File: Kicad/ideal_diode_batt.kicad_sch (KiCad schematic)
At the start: 8 parts, among them Q3 AON7422G, U7 LM74700QDBVTQ1

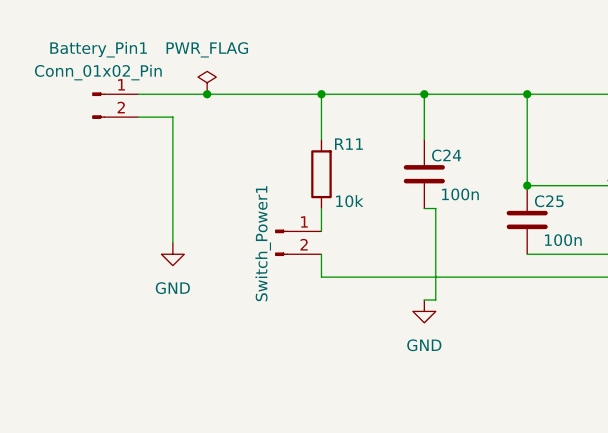
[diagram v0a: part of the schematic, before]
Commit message: finished pcb - added pwm resistors, and fixed VDDA decoupling
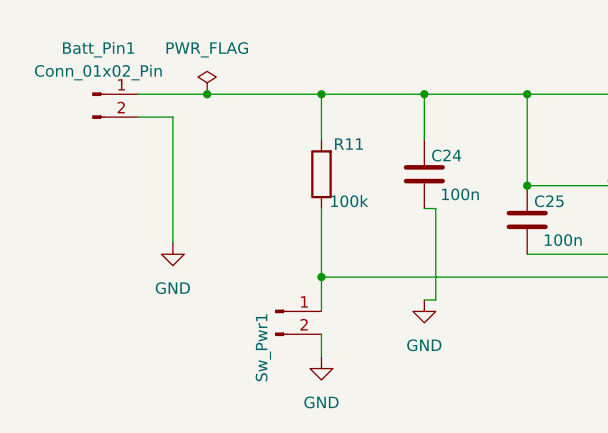
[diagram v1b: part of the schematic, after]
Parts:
- R11: value 10k -> 100k
- renumbered Battery_Pin1 to Batt_Pin1, Switch_Power1 to Sw_Pwr1
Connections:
- net EN: now also R11.1, Sw_Pwr1.1 (Pin_1); no longer Sw_Pwr1.2 (Pin_2)
- net GND: now also Sw_Pwr1.2 (Pin_2)
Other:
- moved on the sheet: Sw_Pwr1
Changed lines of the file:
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@@
+	)
+	(junction
+		(at 91.44 106.68)
+		(diameter 0)
+		(color 0 0 0 0)
 	)
 	(junction
@@
 	(wire
 		(pts
-			(xy 91.44 104.14) (xy 91.44 106.68)
+			(xy 91.44 106.68) (xy 91.44 110.49)
 		)
 		(stroke
@@
 	(wire
 		(pts
+			(xy 91.44 113.03) (xy 91.44 115.57)
+		)
+		(stroke
+			(width 0)
+			(type default)
+		)
+	)
+	(wire
+		(pts
 			(xy 104.14 99.06) (xy 104.14 109.22)
 		)
@@
 	(wire
 		(pts
-			(xy 91.44 99.06) (xy 91.44 101.6)
+			(xy 91.44 99.06) (xy 91.44 106.68)
 		)
 		(stroke
@@
 	(symbol
 		(lib_id "Connector:Conn_01x02_Pin")
-		(at 86.36 101.6 0)
-		(unit 1)
-		(exclude_from_sim no)
-		(in_bom yes)
-		(on_board yes)
-		(dnp no)
-		(property "Reference" "Switch_Power1"
-			(at 84.836 109.474 90)
+		(at 86.36 110.49 0)
+		(unit 1)
+		(exclude_from_sim no)
+		(in_bom yes)
+		(on_board yes)
+		(dnp no)
+		(property "Reference" "Sw_Pwr1"
+			(at 84.836 118.364 90)
 			(effects
 				(font
@@
 		)
 		(property "Value" "Conn_01x02_Pin"
-			(at 88.2649 100.33 90)
+			(at 88.2649 109.22 90)
 			(effects
 				(font
@@
 		)
 		(property "Footprint" "Connector_PinSocket_2.54mm:PinSocket_1x02_P2.54mm_Vertical"
-			(at 86.36 101.6 0)
+			(at 86.36 110.49 0)
 			(effects
 				(font
@@
 		)
 		(property "Datasheet" "~"
-			(at 86.36 101.6 0)
+			(at 86.36 110.49 0)
 			(effects
 				(font
@@
 		)
 		(property "Description" "Generic connector, single row, 01x02, script generated"
-			(at 86.36 101.6 0)
+			(at 86.36 110.49 0)
 			(effects
 				(font
@@
 			(project "MiniSumoSTM"
 				(path "/74ccf643-7ae0-4d9b-8b7c-e7e124cb3f26/5fd6aca6-b06e-4ddc-825d-1f18e20a3d2c/3b4f43c5-65a3-46ea-9ced-7d72115b509a"
-					(reference "Switch_Power1")
+					(reference "Sw_Pwr1")
 					(unit 1)
 				)
@@
 			)
 		)
-		(property "Value" "10k"
+		(property "Value" "100k"
 			(at 94.488 98.298 0)
 			(effects
@@
 		(dnp no)
 		(fields_autoplaced yes)
-		(property "Reference" "Battery_Pin1"
+		(property "Reference" "Batt_Pin1"
 			(at 66.675 81.28 0)
 			(effects
@@
 			(project "MiniSumoSTM"
 				(path "/74ccf643-7ae0-4d9b-8b7c-e7e124cb3f26/5fd6aca6-b06e-4ddc-825d-1f18e20a3d2c/3b4f43c5-65a3-46ea-9ced-7d72115b509a"
-					(reference "Battery_Pin1")
+					(reference "Batt_Pin1")
 					(unit 1)
 				)
@@
 					(unit 1)
 				)
+			)
+		)
+	)
+	(symbol
+		(lib_id "power:GND")
+		(at 91.44 115.57 0)
+		(unit 1)
+		(exclude_from_sim no)
+		(in_bom yes)
+		(on_board yes)
+		(dnp no)
+		(fields_autoplaced yes)
+		(property "Reference" "#PWR067"
+			(at 91.44 121.92 0)
+			(effects
+				(font
+					(size 1.27 1.27)
+				)
+				(hide yes)
+			)
+		)
+		(property "Value" "GND"
+			(at 91.44 120.65 0)
+			(effects
+				(font
+					(size 1.27 1.27)
+				)
+			)
+		)
+		(property "Footprint" ""
+			(at 91.44 115.57 0)
+			(effects
+				(font
+					(size 1.27 1.27)
+				)
+				(hide yes)
+			)
+		)
+		(property "Datasheet" ""
+			(at 91.44 115.57 0)
+			(effects
+				(font
+					(size 1.27 1.27)
+				)
+				(hide yes)
+			)
+		)
+		(property "Description" "Power symbol creates a global label with name \"GND\" , ground"
+			(at 91.44 115.57 0)
+			(effects
+				(font
+					(size 1.27 1.27)
+				)
+				(hide yes)
+			)
+		)
+		(pin "1"
+		)
+		(instances
+			(project "MiniSumoSTM"
+				(path "/74ccf643-7ae0-4d9b-8b7c-e7e124cb3f26/5fd6aca6-b06e-4ddc-825d-1f18e20a3d2c/3b4f43c5-65a3-46ea-9ced-7d72115b509a"
+					(reference "#PWR067")
+					(unit 1)
+				)

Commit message: not small changes
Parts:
- Batt_Pin1, Sw_Pwr1: footprint Connector_PinSocket_2.54mm:PinSocket_1x02_P2.54mm_Vertical -> Connector_PinHeader_2.54mm:PinHeader_1x02_P2.54mm_Vertical
- Q3: footprint Package_DFN_QFN:DFN-8-1EP_3x3mm_P0.5mm_EP1.7x2.4mm -> Package_DFN_QFN:DFN-8-1EP_3x3mm_P0.65mm_EP1.5x2.25mm
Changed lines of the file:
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@@
 			)
 		)
-		(property "Footprint" "Connector_PinSocket_2.54mm:PinSocket_1x02_P2.54mm_Vertical"
+		(property "Footprint" "Connector_PinHeader_2.54mm:PinHeader_1x02_P2.54mm_Vertical"
 			(at 86.36 110.49 0)
 			(effects
@@
 			)
 		)
-		(property "Footprint" "Package_DFN_QFN:DFN-8-1EP_3x3mm_P0.5mm_EP1.7x2.4mm"
+		(property "Footprint" "Package_DFN_QFN:DFN-8-1EP_3x3mm_P0.65mm_EP1.5x2.25mm"
 			(at 167.64 83.82 0)
 			(effects
@@
 			)
 		)
-		(property "Footprint" "Connector_PinSocket_2.54mm:PinSocket_1x02_P2.54mm_Vertical"
+		(property "Footprint" "Connector_PinHeader_2.54mm:PinHeader_1x02_P2.54mm_Vertical"
 			(at 66.04 86.36 0)
 			(effects

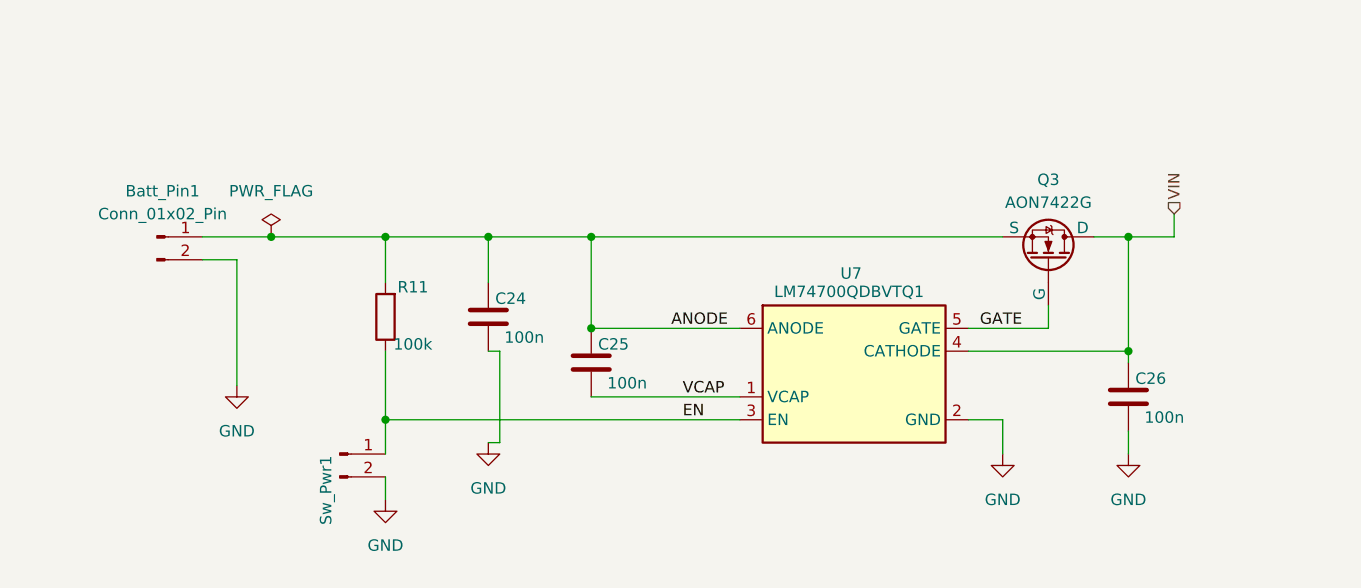
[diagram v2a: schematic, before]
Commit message: kicad schemas documentation
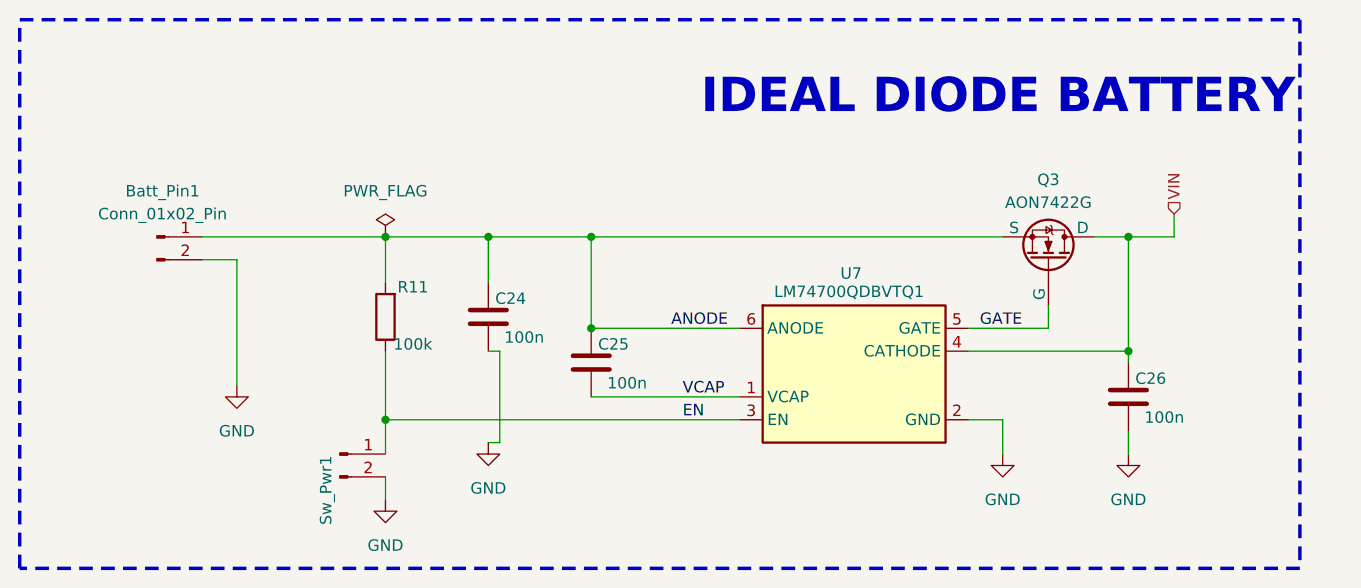
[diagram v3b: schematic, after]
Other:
- note added: "IDEAL DIODE BATTERY"
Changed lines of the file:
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@@
 	(generator_version "9.0")
 	(paper "A4")
+	(rectangle
+		(start 50.8 62.23)
+		(end 193.04 123.19)
+		(stroke
+			(width 0.381)
+			(type dash)
+		)
+		(fill
+			(type none)
+		)
+	)
+	(text "IDEAL DIODE BATTERY\n"
+		(exclude_from_sim no)
+		(at 159.512 70.866 0)
+		(effects
+			(font
+				(size 3.81 3.81)
+				(thickness 0.254)
+				(bold yes)
+			)
+		)
+	)
 	(junction
 		(at 114.3 96.52)
@@
 	)
 	(junction
-		(at 78.74 86.36)
-		(diameter 0)
-		(color 0 0 0 0)
-	)
-	(junction
 		(at 91.44 106.68)
 		(diameter 0)
@@
 	(wire
 		(pts
-			(xy 71.12 86.36) (xy 78.74 86.36)
+			(xy 71.12 86.36) (xy 91.44 86.36)
 		)
 		(stroke
@@
 		(pts
 			(xy 170.18 86.36) (xy 173.99 86.36)
-		)
-		(stroke
-			(width 0)
-			(type default)
-		)
-	)
-	(wire
-		(pts
-			(xy 78.74 86.36) (xy 91.44 86.36)
 		)
 		(stroke
@@
 	(symbol
 		(lib_id "power:PWR_FLAG")
-		(at 78.74 86.36 0)
+		(at 91.44 86.36 0)
 		(unit 1)
 		(exclude_from_sim no)
@@
 		(fields_autoplaced yes)
 		(property "Reference" "#FLG01"
-			(at 78.74 84.455 0)
+			(at 91.44 84.455 0)
 			(effects
 				(font
@@
 		)
 		(property "Value" "PWR_FLAG"
-			(at 78.74 81.28 0)
+			(at 91.44 81.28 0)
 			(effects
 				(font
@@
 		)
 		(property "Footprint" ""
-			(at 78.74 86.36 0)
+			(at 91.44 86.36 0)
 			(effects
 				(font
@@
 		)
 		(property "Datasheet" "~"
-			(at 78.74 86.36 0)
+			(at 91.44 86.36 0)
 			(effects
 				(font
@@
 		)
 		(property "Description" "Special symbol for telling ERC where power comes from"
-			(at 78.74 86.36 0)
-			(effects
-				(font
+			(at 91.44 86.36 0)
+			(effects
+				(font
